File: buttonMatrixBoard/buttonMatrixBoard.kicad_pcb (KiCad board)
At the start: 2 copper layers, 80 x 40 mm, 42 parts, among them J1 Conn_01x04_Pin, J2 Conn_01x02_Pin, J3 Conn_01x02_Pin, J4 Conn_01x04_Pin, J5 Conn_01x04_Pin, J6 Conn_01x03_Pin, SW1 SW_Push, SW2 SW_Push, SW3 SW_Push, SW4 SW_Push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

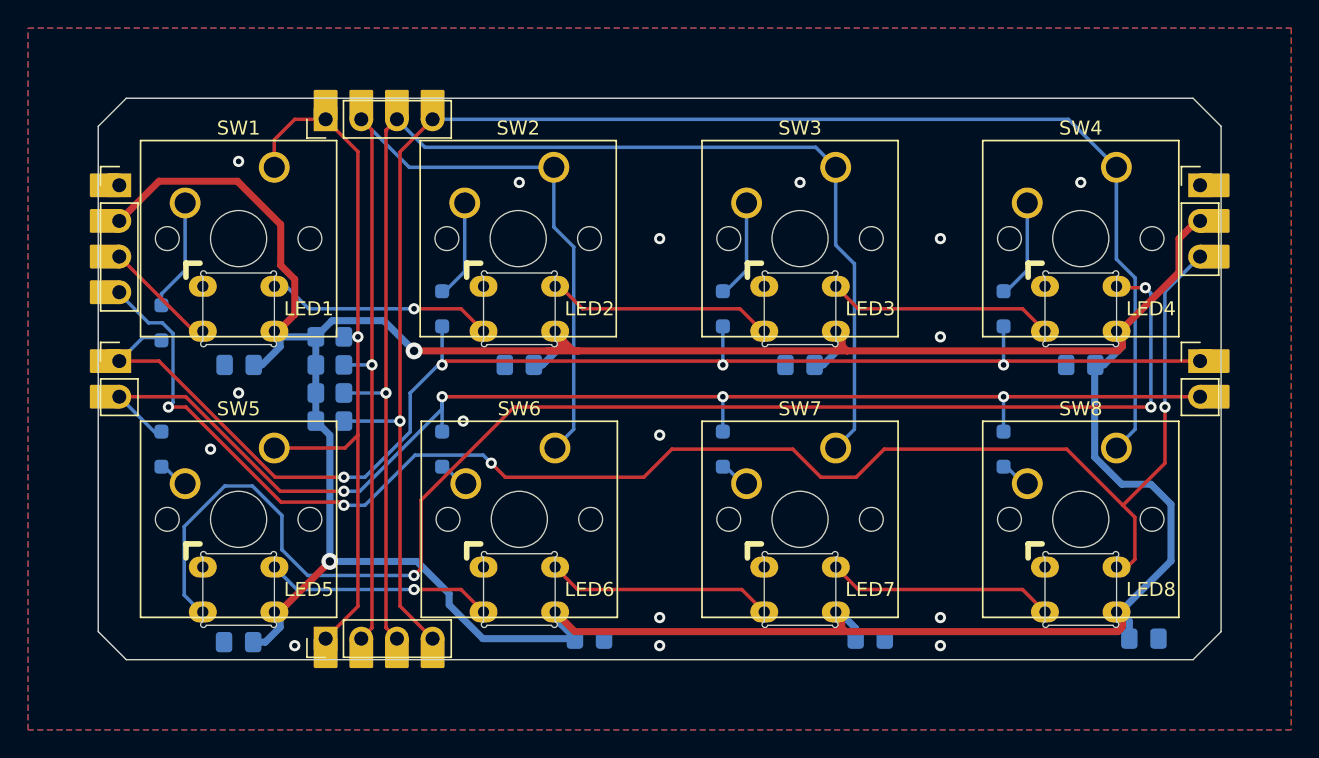
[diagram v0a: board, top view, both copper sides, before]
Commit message: buttonMatrix added mounting holes
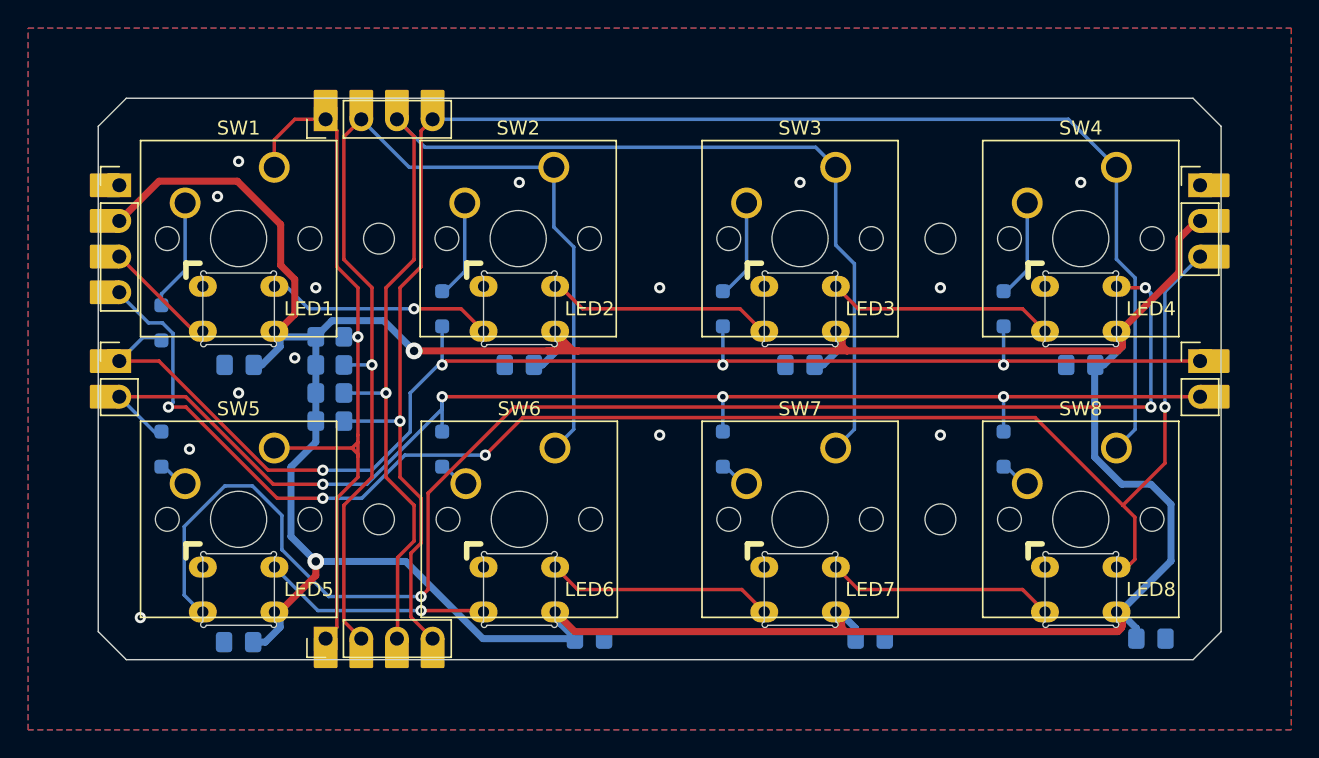
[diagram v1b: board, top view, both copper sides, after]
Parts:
- added REF**: MountingHole_2.2mm_M2, MountingHole:MountingHole_2.2mm_M2, F.Cu at (20.0, 30.0)
- added REF**: MountingHole_2.2mm_M2, MountingHole:MountingHole_2.2mm_M2, F.Cu at (20.0, 10.0)
- added REF**: MountingHole_2.2mm_M2, MountingHole:MountingHole_2.2mm_M2, F.Cu at (60.0, 10.0)
- added REF**: MountingHole_2.2mm_M2, MountingHole:MountingHole_2.2mm_M2, F.Cu at (60.0, 30.0)
- moved C8 0.50 mm to (75.0, 38.5)
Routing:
- net Net-(LED4-DOUT): track 99.4 -> 101.8 mm
- net Sense2: track 75.9 -> 78.0 mm
- net Sense3: track 94.4 -> 96.5 mm
- net Led Out: track 113.3 -> 111.8 mm
- net VCC: track 234.1 -> 235.5 mm
- net Sense4: track 114.2 -> 114.8 mm
- net Sense1: track 52.5 -> 53.0 mm
- net GND: vias 16 -> 14

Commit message: added more edge connections
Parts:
- added ?: , , F.Cu at (74.0, 1.62)
- added ?: , , F.Cu at (75.9, 38.9)
- added ?: , , F.Cu at (78.5, 35.0)
- added ?: , , F.Cu at (1.50, 35.0)
- added ?: , , F.Cu at (6.00, 38.5)
- added ?: , , F.Cu at (4.00, 1.50)
- moved C8 3.54 mm to (75.5, 35.0), turned to 90 degrees
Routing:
- net VCC: track 235.5 -> 233.1 mm
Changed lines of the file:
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@@
   (net 24 "Sense3")
   (net 25 "Sense4")
+  (footprint "" (layer "F.Cu")
+    (at 74 1.625 -90)
+    (fp_text reference "" (at 0 0 90) (layer "F.SilkS")
+        (effects (font (size 1.27 1.27) (thickness 0.15)))
+    )
+    (fp_text value "" (at 0 0 90) (layer "F.SilkS")
+        (effects (font (size 1.27 1.27) (thickness 0.15)))
+    )
+    (pad "1" thru_hole custom (at -0.125 -2 270) (size 1.7 1.7) (drill 1) (layers "*.Cu" "*.Mask")
+      (net 13 "GND") (pinfunction "Pin_1") (pintype "passive")
+      (options (clearance outline) (anchor rect))
+      (primitives
+        (gr_poly
+          (pts
+            (xy 0 -0.75)
+            (xy -2 -0.75)
+            (xy -2 0.75)
+            (xy 0 0.75)
+          )
+          (width 0.2) (fill yes))
+      ))
+  )
   (footprint "Button_Switch_Keyboard:SW_Cherry_MX_1.00u_PCB" locked (layer "F.Cu")
     (at 32.54 24.92)
@@
     )
   )
+  (footprint "" (layer "F.Cu")
+    (at 75.9 38.875 90)
+    (fp_text reference "" (at 0 0 90) (layer "F.SilkS")
+        (effects (font (size 1.27 1.27) (thickness 0.15)))
+    )
+    (fp_text value "" (at 0 0 90) (layer "F.SilkS")
+        (effects (font (size 1.27 1.27) (thickness 0.15)))
+    )
+    (pad "1" thru_hole custom (at 0.375 0.1 90) (size 1.7 1.7) (drill 1) (layers "*.Cu" "*.Mask")
+      (net 13 "GND") (pinfunction "Pin_1") (pintype "passive")
+      (options (clearance outline) (anchor rect))
+      (primitives
+        (gr_poly
+          (pts
+            (xy 0 -0.75)
+            (xy -2 -0.75)
+            (xy -2 0.75)
+            (xy 0 0.75)
+          )
+          (width 0.2) (fill yes))
+      ))
+  )
   (footprint "Library:WS2812_embedded" locked (layer "F.Cu")
     (at 30 35 180)
@@
     (pad "" np_thru_hole circle (at 0 0) (size 2.2 2.2) (drill 2.2) (layers "F&B.Cu" "*.Mask"))
   )
+  (footprint "" (layer "F.Cu")
+    (at 78.5 35 180)
+    (fp_text reference "" (at 0 0) (layer "F.SilkS")
+        (effects (font (size 1.27 1.27) (thickness 0.15)))
+    )
+    (fp_text value "" (at 0 0) (layer "F.SilkS")
+        (effects (font (size 1.27 1.27) (thickness 0.15)))
+    )
+    (pad "1" thru_hole custom (at 0.375 -1.2 180) (size 1.7 1.7) (drill 1) (layers "*.Cu" "*.Mask")
+      (net 13 "GND") (pinfunction "Pin_1") (pintype "passive")
+      (options (clearance outline) (anchor rect))
+      (primitives
+        (gr_poly
+          (pts
+            (xy 0 -0.75)
+            (xy -2 -0.75)
+            (xy -2 0.75)
+            (xy 0 0.75)
+          )
+          (width 0.2) (fill yes))
+      ))
+  )
   (footprint "MountingHole:MountingHole_2.2mm_M2" (layer "F.Cu")
     (at 60 10)
@@
         (effects (font (size 1 1) (thickness 0.1)))
     )
-    (fp_text value "WS2812B" (at -15.02 -45.95 180 unlocked) (layer "F.Fab")
+    (fp_text value "WS2812B" (at 0 -5.75 180 unlocked) (layer "F.Fab")
         (effects (font (size 1 1) (thickness 0.15)))
     )
@@
     )
   )
+  (footprint "" (layer "F.Cu")
+    (at 1.5 35)
+    (fp_text reference "" (at 0 0) (layer "F.SilkS")
+        (effects (font (size 1.27 1.27) (thickness 0.15)))
+    )
+    (fp_text value "" (at 0 0) (layer "F.SilkS")
+        (effects (font (size 1.27 1.27) (thickness 0.15)))
+    )
+    (pad "1" thru_hole custom (at 0 -1.2) (size 1.7 1.7) (drill 1) (layers "*.Cu" "*.Mask")
+      (net 13 "GND") (pinfunction "Pin_1") (pintype "passive")
+      (options (clearance outline) (anchor rect))
+      (primitives
+        (gr_poly
+          (pts
+            (xy 0 -0.75)
+            (xy -2 -0.75)
+            (xy -2 0.75)
+            (xy 0 0.75)
+          )
+          (width 0.2) (fill yes))
+      ))
+  )
   (footprint "Button_Switch_Keyboard:SW_Cherry_MX_1.00u_PCB" locked (layer "F.Cu")
     (at 52.54 4.92)
@@
     )
   )
+  (footprint "" (layer "F.Cu")
+    (at 6 38.5 90)
+    (fp_text reference "" (at 0 0 90) (layer "F.SilkS")
+        (effects (font (size 1.27 1.27) (thickness 0.15)))
+    )
+    (fp_text value "" (at 0 0 90) (layer "F.SilkS")
+        (effects (font (size 1.27 1.27) (thickness 0.15)))
+    )
+    (pad "1" thru_hole custom (at 0 -2 90) (size 1.7 1.7) (drill 1) (layers "*.Cu" "*.Mask")
+      (net 13 "GND") (pinfunction "Pin_1") (pintype "passive")
+      (options (clearance outline) (anchor rect))
+      (primitives
+        (gr_poly
+          (pts
+            (xy 0 -0.75)
+            (xy -2 -0.75)
+            (xy -2 0.75)
+            (xy 0 0.75)
+          )
+          (width 0.2) (fill yes))
+      ))
+  )
   (footprint "Button_Switch_Keyboard:SW_Cherry_MX_1.00u_PCB" locked (layer "F.Cu")
     (at 52.54 24.92)
@@
     )
   )
+  (footprint "" (layer "F.Cu")
+    (at 4 1.5 -90)
+    (fp_text reference "" (at 0 0 90) (layer "F.SilkS")
+        (effects (font (size 1.27 1.27) (thickness 0.15)))
+    )
+    (fp_text value "" (at 0 0 90) (layer "F.SilkS")
+        (effects (font (size 1.27 1.27) (thickness 0.15)))
+    )
+    (pad "1" thru_hole custom (at 0 -2 270) (size 1.7 1.7) (drill 1) (layers "*.Cu" "*.Mask")
+      (net 13 "GND") (pinfunction "Pin_1") (pintype "passive")
+      (options (clearance outline) (anchor rect))
+      (primitives
+        (gr_poly
+          (pts
+            (xy 0 -0.75)
+            (xy -2 -0.75)
+            (xy -2 0.75)
+            (xy 0 0.75)
+          )
+          (width 0.2) (fill yes))
+      ))
+  )
   (footprint "Button_Switch_Keyboard:SW_Cherry_MX_1.00u_PCB" locked (layer "F.Cu")
     (at 72.54 24.92)
@@
   )
   (footprint "Capacitor_SMD:C_0805_2012Metric_Pad1.18x1.45mm_HandSolder" (layer "B.Cu")
-    (at 75 38.5 180)
+    (at 75.5 35 90)
     (descr "Capacitor SMD 0805 (2012 Metric), square (rectangular) end terminal, IPC_7351 nominal with elongated pad for handsoldering. (Body size source: IPC-SM-782 page 76, https://www.pcb-3d.com/wordpress/wp-content/uploads/ipc-sm-782a_amendment_1_and_2.pdf, https://docs.google.com/spreadsheets/d/1BsfQQcO9C6DZCsRaXUlFlo91Tg2WpOkGARC1WS5S8t0/edit?usp=sharing), generated with kicad-footprint-generator")
     (tags "capacitor handsolder")
@@
     (property "ki_keywords" "cap capacitor")
     (attr smd)
-    (fp_text reference "C8" (at 3 0) (layer "B.SilkS")
+    (fp_text reference "C8" (at 2.5 0 180) (layer "B.SilkS")
         (effects (font (size 1 1) (thickness 0.15)) (justify mirror))
     )
-    (fp_text value "100nF" (at 0 -1.68) (layer "B.Fab")
+    (fp_text value "100nF" (at 0 -1.68 90) (layer "B.Fab")
         (effects (font (size 1 1) (thickness 0.15)) (justify mirror))
     )
-    (fp_text user "${REFERENCE}" (at 0 0) (layer "B.Fab")
+    (fp_text user "${REFERENCE}" (at 0 0 90) (layer "B.Fab")
         (effects (font (size 0.5 0.5) (thickness 0.08)) (justify mirror))
     )
@@
     (fp_line (start 1 0.625) (end 1 -0.625)
       (stroke (width 0.1) (type solid)) (layer "B.Fab"))
-    (pad "1" smd roundrect (at -1.0375 0 180) (size 1.175 1.45) (layers "B.Cu" "B.Paste" "B.Mask") (roundrect_rratio 0.212766)
+    (pad "1" smd roundrect (at -1.0375 0 90) (size 1.175 1.45) (layers "B.Cu" "B.Paste" "B.Mask") (roundrect_rratio 0.212766)
       (net 13 "GND") (pintype "passive"))
-    (pad "2" smd roundrect (at 1.0375 0 180) (size 1.175 1.45) (layers "B.Cu" "B.Paste" "B.Mask") (roundrect_rratio 0.212766)
+    (pad "2" smd roundrect (at 1.0375 0 90) (size 1.175 1.45) (layers "B.Cu" "B.Paste" "B.Mask") (roundrect_rratio 0.212766)
       (net 11 "VCC") (pintype "passive"))
     (model "${KICAD6_3DMODEL_DIR}/Capacitor_SMD.3dshapes/C_0805_2012Metric.wrl"
@@
   (segment (start 13.2 17) (end 12.964179 16.764179) (width 0.5) (layer "B.Cu") (net 11))
   (segment (start 15.5 33) (end 13.73 31.23) (width 0.5) (layer "B.Cu") (net 11))
-  (segment (start 73.9625 37.7625) (end 72.8 36.6) (width 0.5) (layer "B.Cu") (net 11))
   (segment (start 11.6625 19) (end 11.075 19) (width 0.5) (layer "B.Cu") (net 11))
   (segment (start 15.5 33) (end 21.902944 33) (width 0.5) (layer "B.Cu") (net 11))
@@
   (segment (start 21.902944 33) (end 27.402944 38.5) (width 0.5) (layer "B.Cu") (net 11))
   (segment (start 16.65 15.85) (end 20.35 15.85) (width 0.5) (layer "B.Cu") (net 11))
-  (segment (start 73.9625 38.5) (end 73.9625 37.7625) (width 0.5) (layer "B.Cu") (net 11))
   (segment (start 71.649363 19) (end 72.964179 17.685184) (width 0.5) (layer "B.Cu") (net 11))
   (segment (start 27.402944 38.5) (end 33.9625 38.5) (width 0.5) (layer "B.Cu") (net 11))

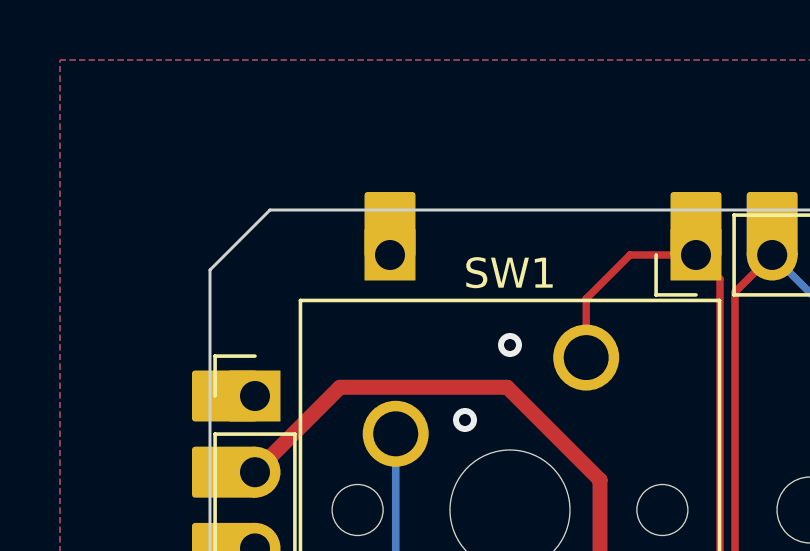
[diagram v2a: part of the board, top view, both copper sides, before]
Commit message: updated pannel and ibom
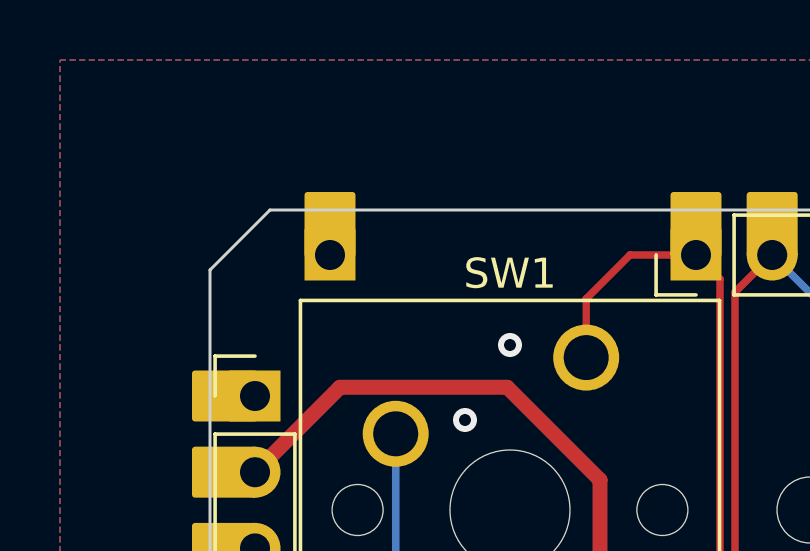
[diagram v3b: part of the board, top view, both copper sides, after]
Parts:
- moved ? 1.80 mm to (2.20, 1.50)
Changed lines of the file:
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@@
   )
   (footprint "" (layer "F.Cu")
-    (at 4 1.5 -90)
+    (at 2.2 1.5 -90)
     (fp_text reference "" (at 0 0 90) (layer "F.SilkS")
         (effects (font (size 1.27 1.27) (thickness 0.15)))
@@
         (effects (font (size 1.27 1.27) (thickness 0.15)))
     )
-    (pad "1" thru_hole custom (at 0 -2 270) (size 1.7 1.7) (drill 1) (layers "*.Cu" "*.Mask")
+    (pad "1" thru_hole custom (at 0 -1.8 270) (size 1.7 1.7) (drill 1) (layers "*.Cu" "*.Mask")
       (net 13 "GND") (pinfunction "Pin_1") (pintype "passive")
       (options (clearance outline) (anchor rect))

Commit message: some updates
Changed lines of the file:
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@@
         (effects (font (size 1.27 1.27) (thickness 0.15)))
     )
-    (pad "1" thru_hole custom (at 0.375 -1.2 180) (size 1.7 1.7) (drill 1) (layers "*.Cu" "*.Mask")
+    (pad "1" thru_hole custom (at 0.375 1.2 180) (size 1.7 1.7) (drill 1) (layers "*.Cu" "*.Mask")
       (net 13 "GND") (pinfunction "Pin_1") (pintype "passive")
       (options (clearance outline) (anchor rect))
